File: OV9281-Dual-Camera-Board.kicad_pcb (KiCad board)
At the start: 4 copper layers, 100 x 25 mm, 80 parts, among them IC1 TLV73328PDBVT, IC2 TLV73318PDBVT, IC3 TLV73312PDBVT, J3 WE_68715014522, Q1 BSS138AKA, U1 OV9281, U2 OV9281, U3 NTS0104BQ, U4 NTB0104BQ, Y1 7C-24.000MBB-T, Y2 7C-24.000MBB-T

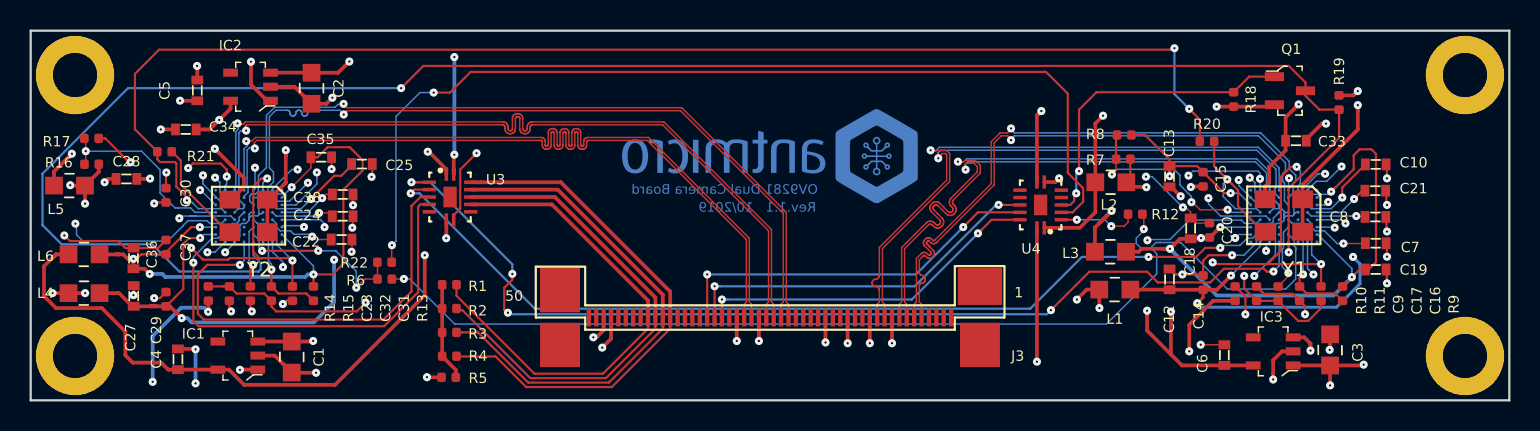
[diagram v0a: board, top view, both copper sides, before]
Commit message: Added OSHW logo, updated hole spacing for lens mount
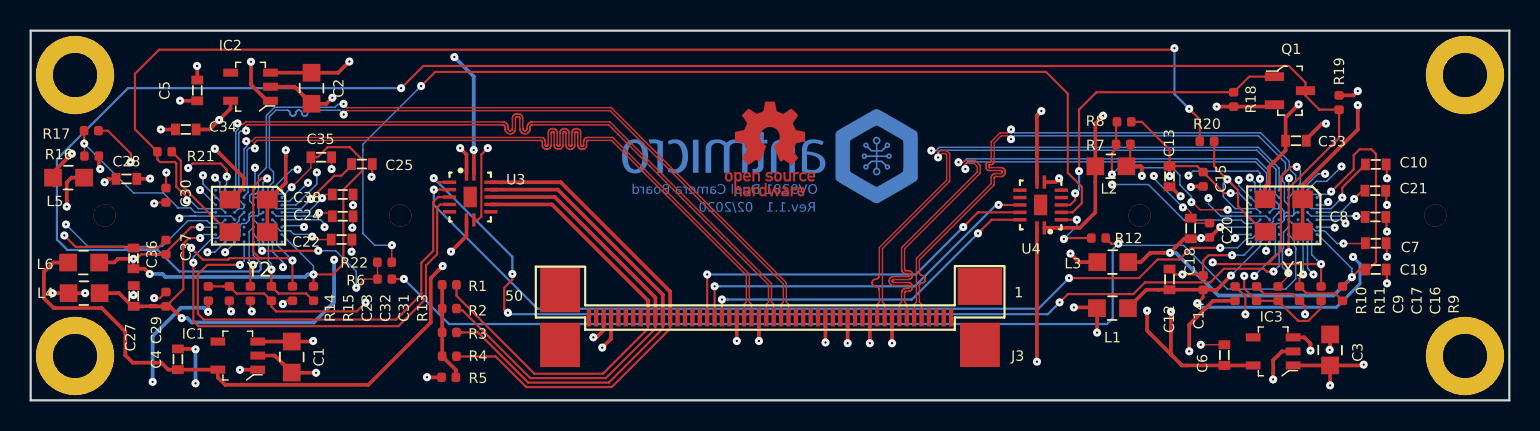
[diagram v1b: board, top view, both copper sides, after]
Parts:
- added MP5: Camera_Lens, antmicro-footprints:Camera_Lens_20mm, B.Cu at (115.0, 112.5)
- added MP6: Camera_Lens, antmicro-footprints:Camera_Lens_20mm, B.Cu at (185.0, 112.5)
- added N2: oshw_logo, antmicro-footprints:oshw-logo, F.Cu at (150.0, 108.0)
- Y1, Y2: value 7C-24.000MBB-T -> Farnell_1842027
- moved R12 2.96 mm to (172.2, 114.0)
- moved U3 1.36 mm to (129.7, 111.2)
- moved L1 1.27 mm to (173.2, 118.8)
- moved L2 1.08 mm to (173.1, 109.2)
- moved R7 1.00 mm to (173.9, 107.7)
- moved R8 0.89 mm to (173.9, 106.2)
- moved L3 0.72 mm to (173.2, 115.7)
- moved R16 0.55 mm to (104.1, 108.5)
- moved L6 0.55 mm to (103.6, 115.7)
- moved L5 0.54 mm to (102.6, 109.9)
- moved R17 0.52 mm to (104.1, 106.8)
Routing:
- net /CAM_R_D1_P: track 52.5 -> 49.7 mm
- net /CAM_R_D1_N: track 52.5 -> 49.7 mm
- net /M2_VSYNC_1V8: track 66.9 -> 69.3 mm
- net /M1_AGND: track 30.0 -> 32.4 mm
- net /CAM_R_D0_N: track 52.4 -> 50.3 mm
- net /CAM_R_D0_P: track 52.3 -> 50.2 mm
- net +2V8: track 43.4 -> 41.6 mm
- net /M1_CAM_SDA_1V8: track 69.4 -> 67.6 mm
- net /M1_VSYNC_1V8_M: track 74.7 -> 73.3 mm
- net /CAM_R_CLK_P: track 52.8 -> 51.3 mm
- net /CAM_R_CLK_N: track 52.8 -> 51.4 mm
- net /M2_CAM_SCL: track 33.7 -> 32.4 mm
- net /M1_CAM_SCL: track 35.1 -> 33.7 mm
- net /M2_CAM_SDA: track 34.2 -> 32.8 mm
- net /M1_CAM_SDA: track 36.0 -> 34.6 mm
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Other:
- board text added: "Rev.1.1 02/2020"
- board text removed: "Rev.1.1 10/2019"
